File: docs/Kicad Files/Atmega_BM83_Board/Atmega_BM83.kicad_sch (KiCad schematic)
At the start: 7 parts, among them J1 Conn_01x12, J2 Conn_01x12, U1 ATmega328P-P

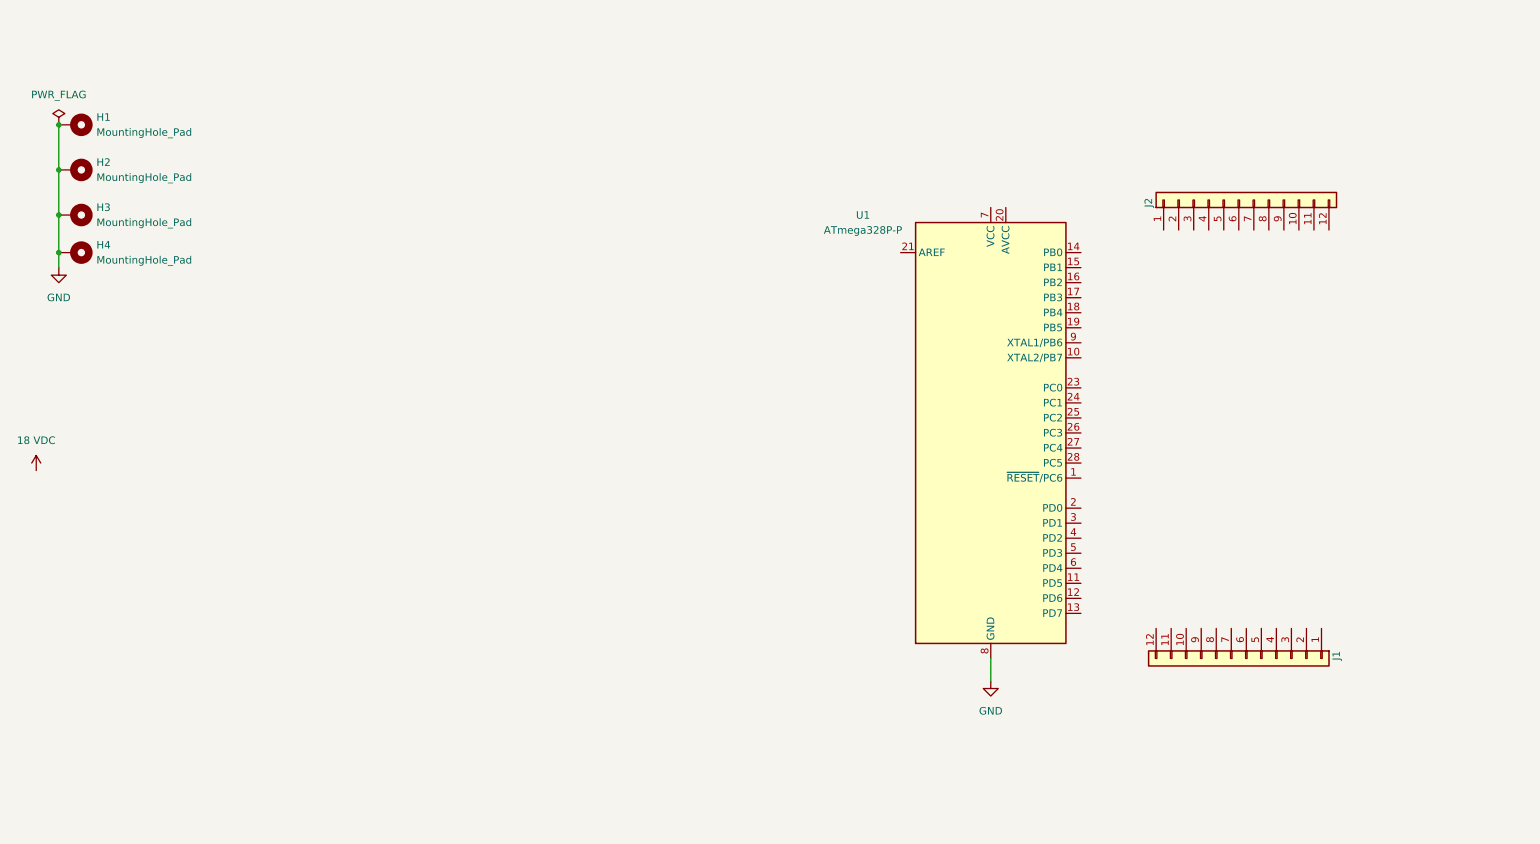
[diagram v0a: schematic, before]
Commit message: Added voltage divider
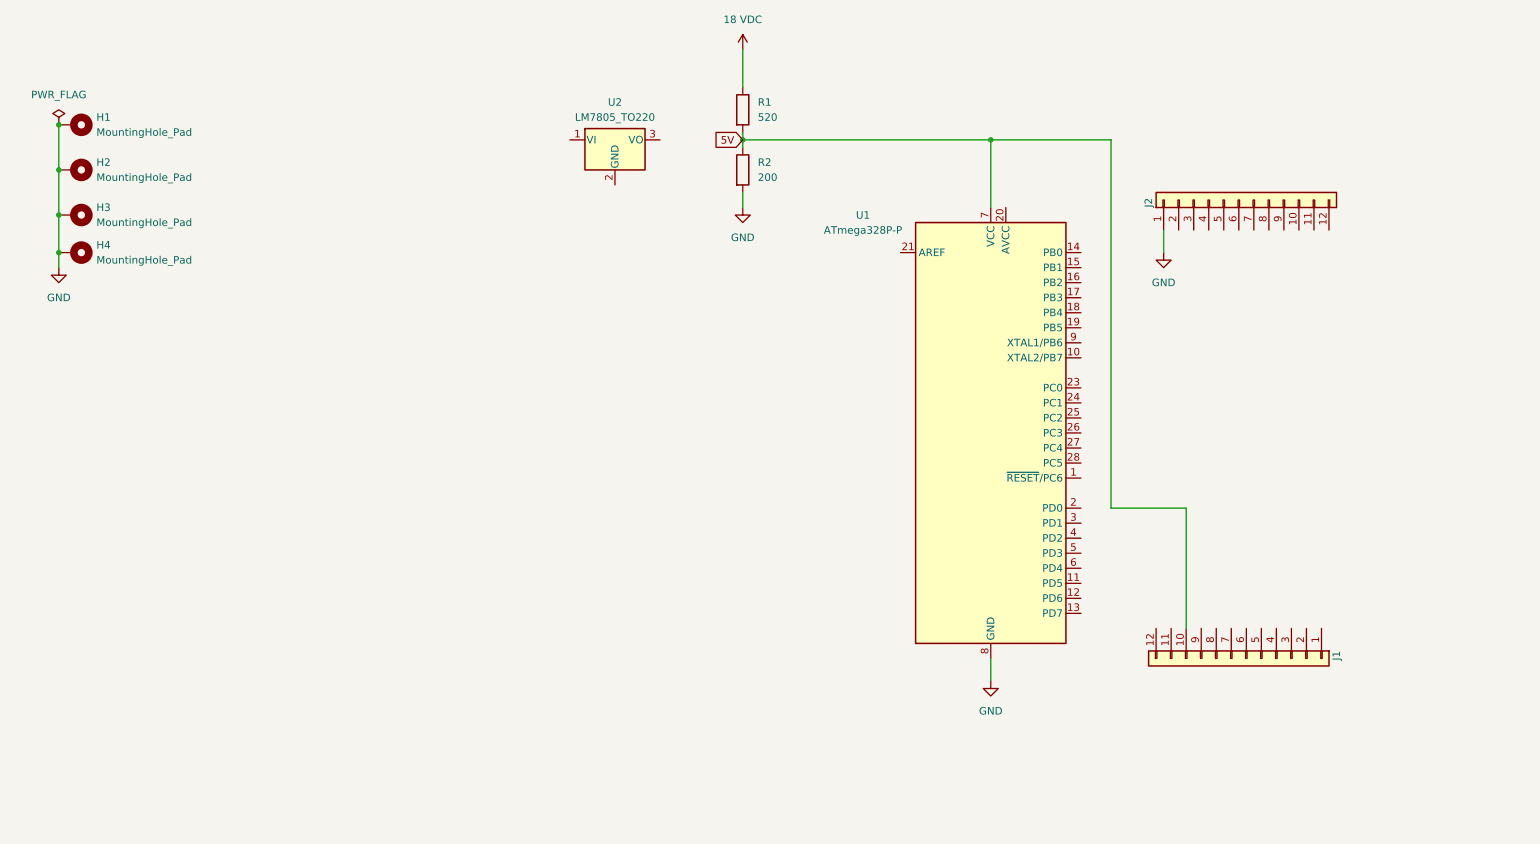
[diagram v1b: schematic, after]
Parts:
- added R1: 520, symbol Device:R
- added R2: 200, symbol Device:R
- added U2: LM7805_TO220, Package_TO_SOT_THT:TO-220-3_Vertical, symbol Regulator_Linear:LM7805_TO220
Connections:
- net 18 VDC: now also R1.1
- net GND: now also J2.1 (Pin_1), R2.2
- net 5V: now reaches J1.10 (Pin_10)
- net 5V: now also U1.7 (VCC), R1.2, R2.1

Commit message: updates for BM83/Atmega schematic
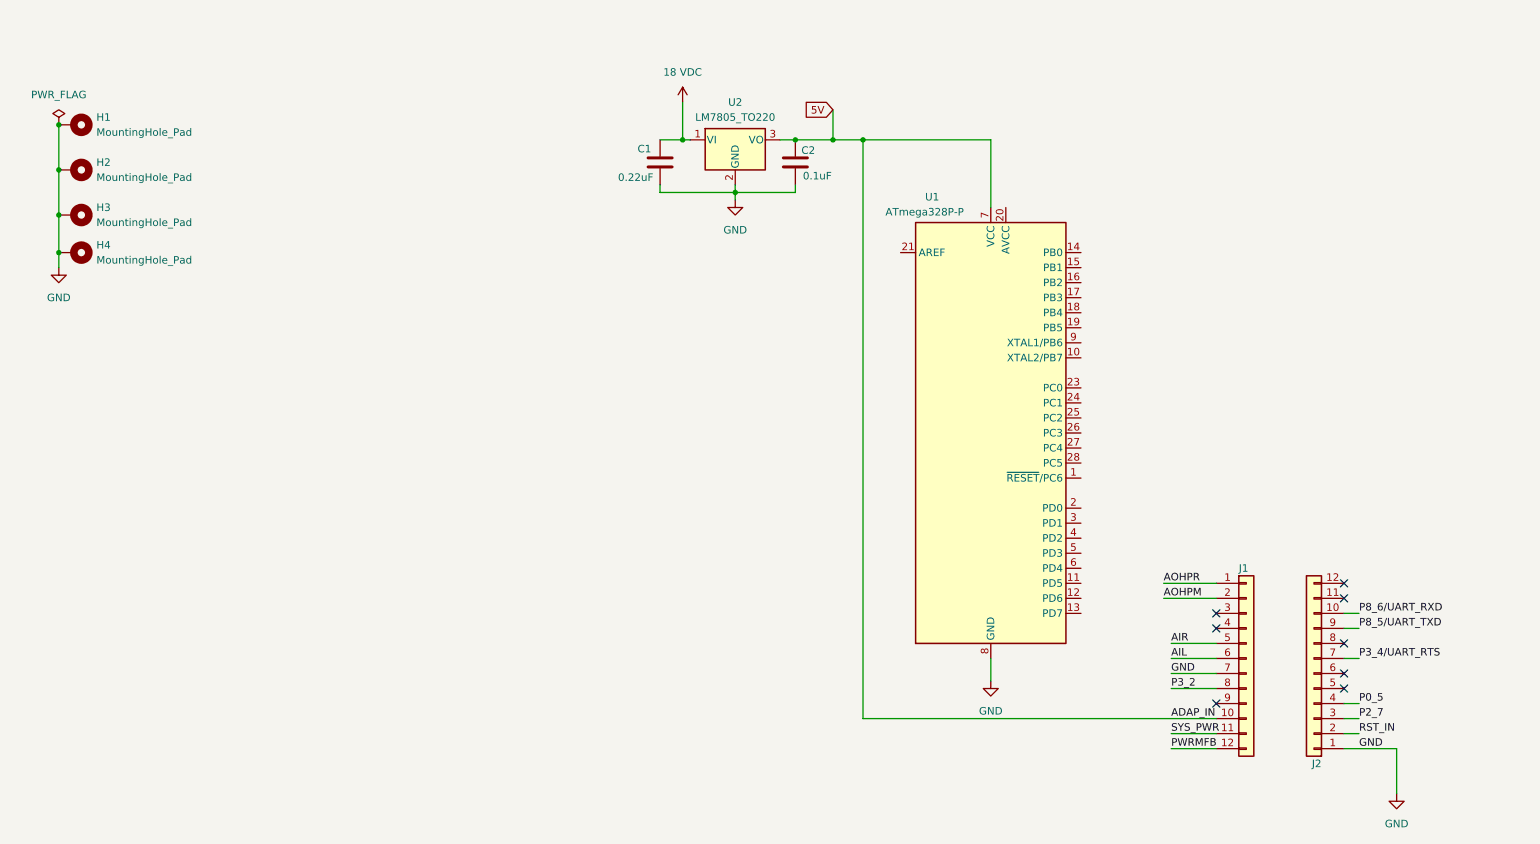
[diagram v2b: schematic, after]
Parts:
- removed R1: 520, symbol Device:R
- removed R2: 200, symbol Device:R
- added C1: 0.22uF, symbol Device:C
- added C2: 0.1uF, symbol Device:C
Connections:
- net 18 VDC: now also U2.1 (VI), C1.1
- net 5V: now also U2.3 (VO), C2.1
- net GND: now also J1.7 (Pin_7), U2.2 (GND), C1.2, C2.2
- net P8_6/UART_RXD: now reaches J2.10 (Pin_10)
- net RST_IN: now reaches J2.2 (Pin_2)
- net P2_7: now reaches J2.3 (Pin_3)
- net P0_5: now reaches J2.4 (Pin_4)
- net P3_4/UART_RTS: now reaches J2.7 (Pin_7)
- net P8_5/UART_TXD: now reaches J2.9 (Pin_9)
- net AOHPR: now reaches J1.1 (Pin_1)
- net SYS_PWR: now reaches J1.11 (Pin_11)
- net PWRMFB: now reaches J1.12 (Pin_12)
- net AOHPM: now reaches J1.2 (Pin_2)
- net AIR: now reaches J1.5 (Pin_5)
- net AIL: now reaches J1.6 (Pin_6)
- net P3_2: now reaches J1.8 (Pin_8)
- no-connect marks 0 -> 8
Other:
- moved on the sheet: J1, J2, U2

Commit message: more work on BM83/Atmega schematic
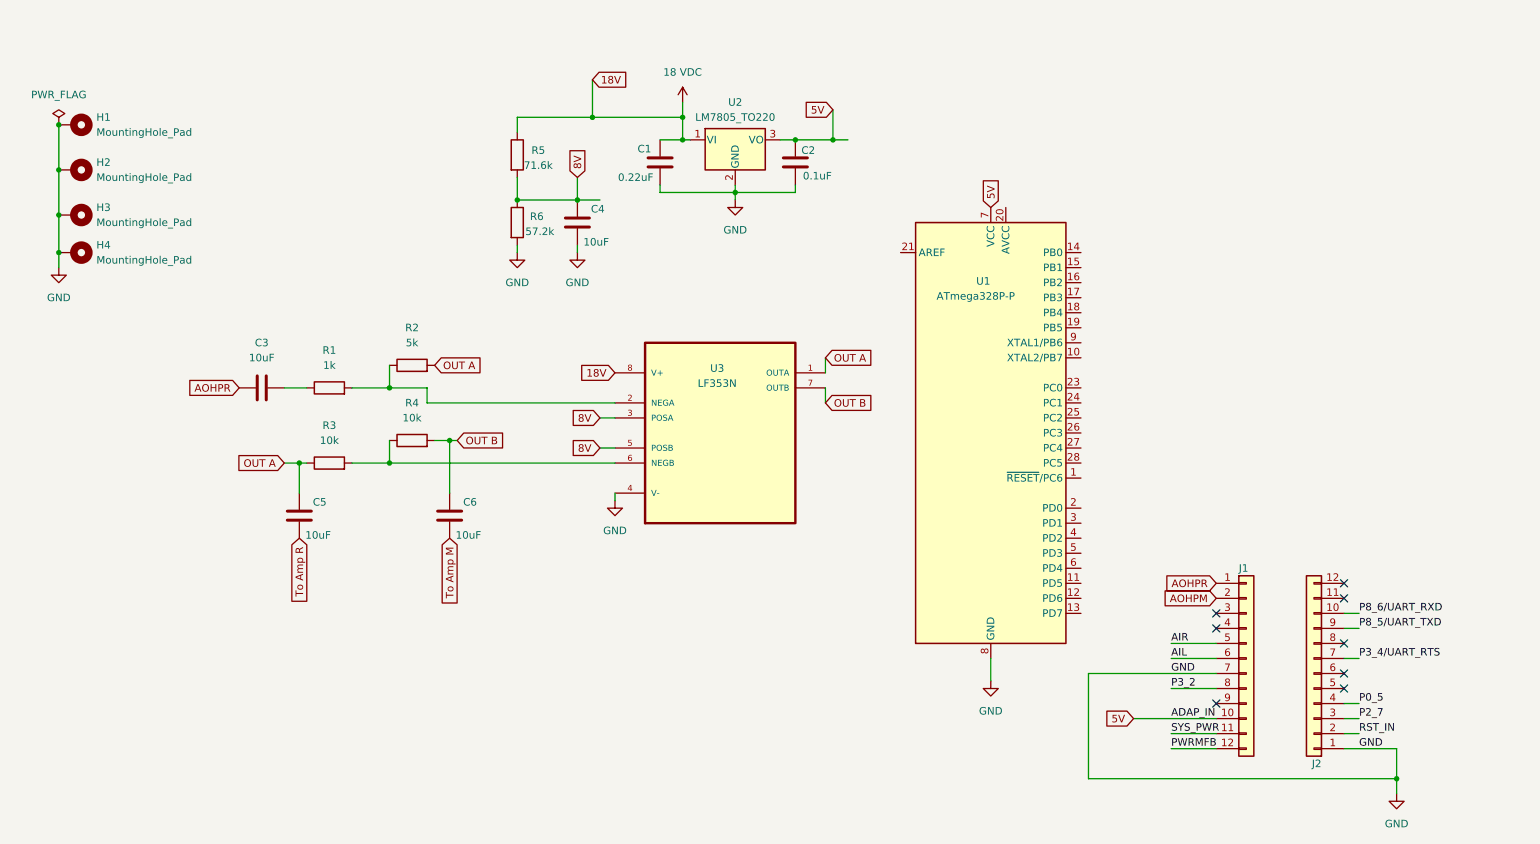
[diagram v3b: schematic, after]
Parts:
- added C3, C4, C5, C6: 10uF, symbol Device:C
- added R1: 1k, symbol Device:R
- added R2: 5k, symbol Device:R
- added R3, R4: 10k, symbol Device:R
- added R5: 71.6k, symbol Device:R
- added R6: 57.2k, symbol Device:R
- added U3: LF353N, Z_Custom_Footprints:LF353, symbol LF353N:LF353N
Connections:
- net 18 VDC: now also R5.1, U3.8 (V+)
- net AOHPR: now also C3.1
- net GND: now also C4.1, R6.2, U3.4 (V-)
- new net: R3.2, R4.1, U3.6 (NEGB)
- new net: R1.2, R2.1, U3.2 (NEGA)
- new net: C3.2, R1.1
- new net 8V: C4.2, R5.2, R6.1, U3.3 (POSA), U3.5 (POSB)
- new net OUT A: C5.2, R2.2, R3.1, U3.1 (OUTA)
- new net OUT B: C6.2, R4.2, U3.7 (OUTB)
- new net To Amp M: C6.1
- new net To Amp R: C5.1

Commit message: more work on BM83/Atmega schematic
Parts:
- added R7, R8: ~, symbol Device:R
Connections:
- net 18 VDC: now also R7.1; no longer U3.8 (V+)
- net GND: now also R8.2
- new net 16V: R7.2, R8.1, U3.8 (V+)

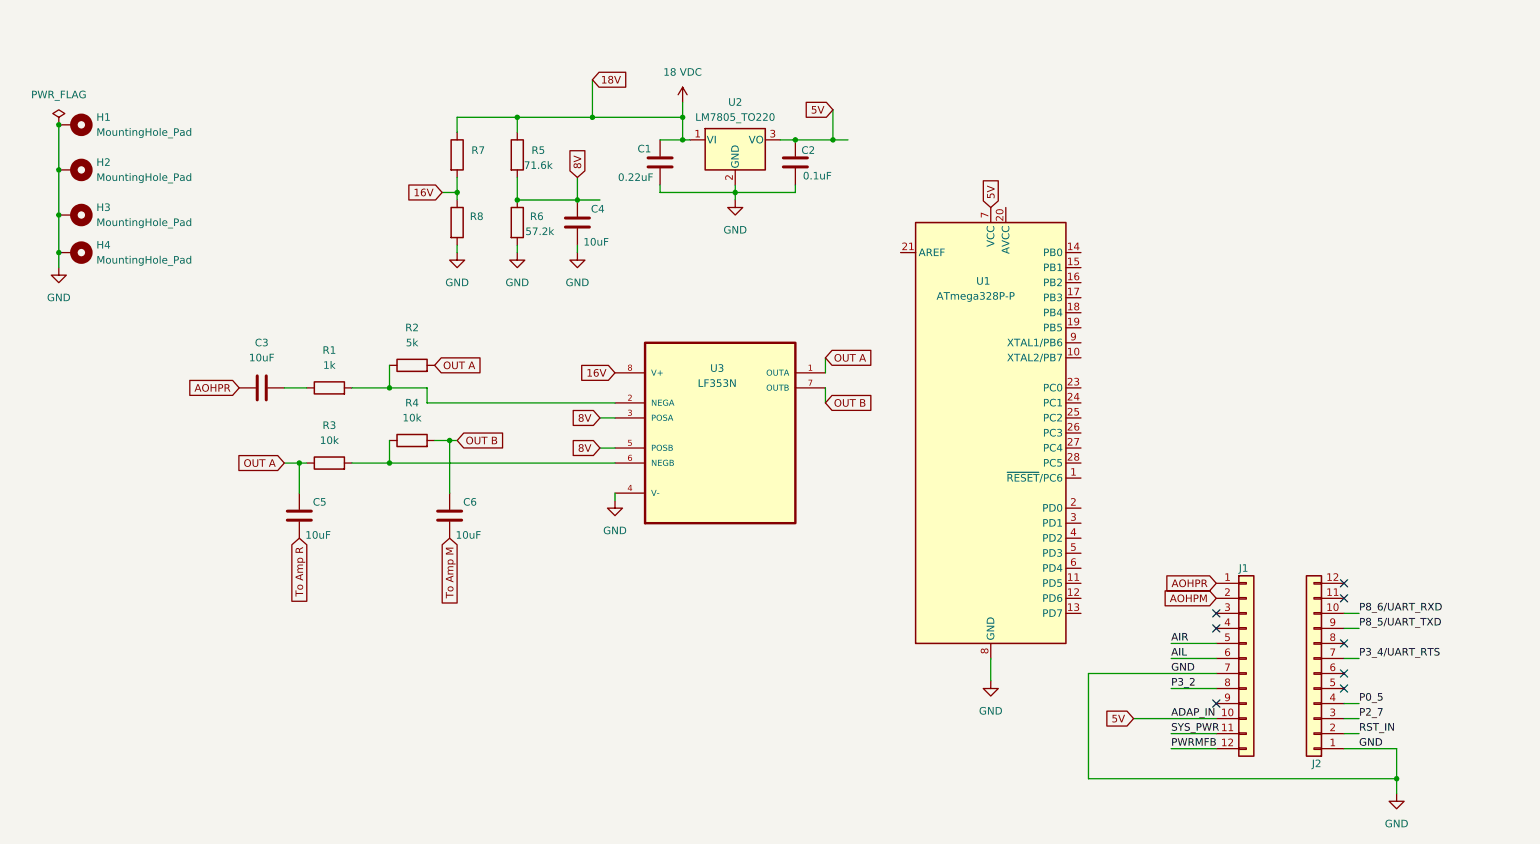
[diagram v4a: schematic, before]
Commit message: more work on Atmega/BM83 schematic
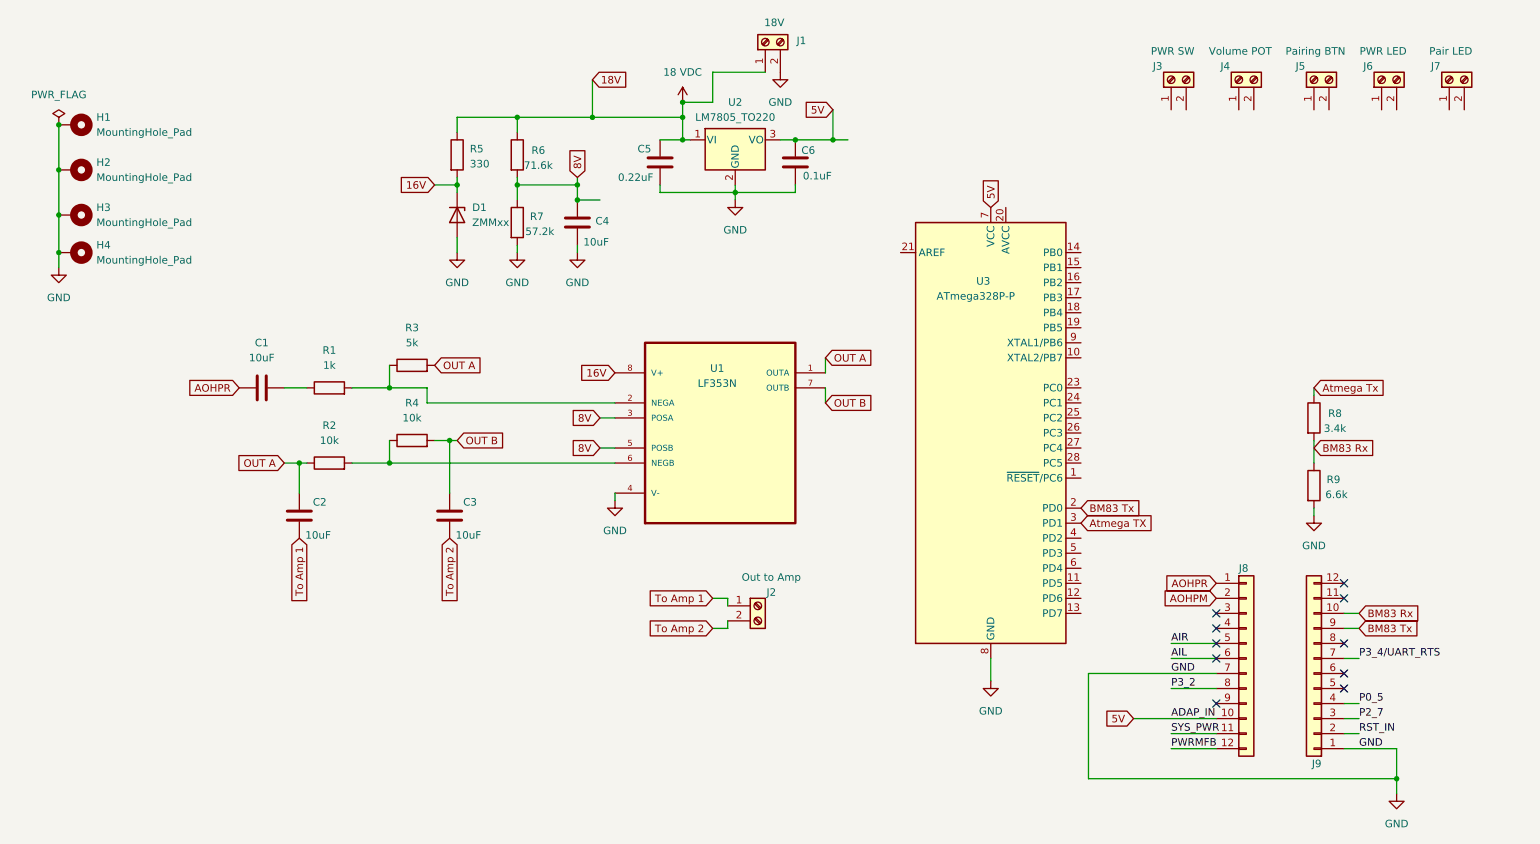
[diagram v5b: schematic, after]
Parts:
- removed R7: ~, symbol Device:R
- added D1: ZMMxx, Diode_SMD:D_MiniMELF, symbol Diode:ZMMxx
- added J1: 18V, TerminalBlock_Phoenix:TerminalBlock_Phoenix_MKDS-1,5-2_1x02_P5.00mm_Horizontal, symbol Connector:Screw_Terminal_01x02
- added J2: Out to Amp, TerminalBlock_Phoenix:TerminalBlock_Phoenix_MKDS-1,5-2_1x02_P5.00mm_Horizontal, symbol Connector:Screw_Terminal_01x02
- added J3: PWR SW, TerminalBlock_Phoenix:TerminalBlock_Phoenix_MKDS-1,5-2_1x02_P5.00mm_Horizontal, symbol Connector:Screw_Terminal_01x02
- added J4: Volume POT, TerminalBlock_Phoenix:TerminalBlock_Phoenix_MKDS-1,5-2_1x02_P5.00mm_Horizontal, symbol Connector:Screw_Terminal_01x02
- added J5: Pairing BTN, TerminalBlock_Phoenix:TerminalBlock_Phoenix_MKDS-1,5-2_1x02_P5.00mm_Horizontal, symbol Connector:Screw_Terminal_01x02
- added J6: PWR LED, TerminalBlock_Phoenix:TerminalBlock_Phoenix_MKDS-1,5-2_1x02_P5.00mm_Horizontal, symbol Connector:Screw_Terminal_01x02
- added J7: Pair LED, TerminalBlock_Phoenix:TerminalBlock_Phoenix_MKDS-1,5-2_1x02_P5.00mm_Horizontal, symbol Connector:Screw_Terminal_01x02
- added R8: 3.4k, Resistor_THT:R_Axial_DIN0207_L6.3mm_D2.5mm_P10.16mm_Horizontal, symbol Device:R
- added R9: 6.6k, Resistor_THT:R_Axial_DIN0207_L6.3mm_D2.5mm_P10.16mm_Horizontal, symbol Device:R
- C5: renamed from C1; footprint (none) -> Capacitor_THT:C_Rect_L7.0mm_W3.5mm_P5.00mm
- R1, R4: footprint (none) -> Resistor_THT:R_Axial_DIN0207_L6.3mm_D2.5mm_P10.16mm_Horizontal
- R2: renamed from R3; footprint (none) -> Resistor_THT:R_Axial_DIN0207_L6.3mm_D2.5mm_P10.16mm_Horizontal
- R3: renamed from R2; footprint (none) -> Resistor_THT:R_Axial_DIN0207_L6.3mm_D2.5mm_P10.16mm_Horizontal
- R5: renamed from R8; value ~ -> 330; footprint (none) -> Resistor_THT:R_Axial_DIN0207_L6.3mm_D2.5mm_P10.16mm_Horizontal
- R6: renamed from R5; footprint (none) -> Resistor_THT:R_Axial_DIN0207_L6.3mm_D2.5mm_P10.16mm_Horizontal
- R7: renamed from R6; footprint (none) -> Resistor_THT:R_Axial_DIN0207_L6.3mm_D2.5mm_P10.16mm_Horizontal
- renumbered C3 to C1, C5 to C2, C6 to C3, C2 to C6, J1 to J8, J2 to J9, U3 to U1, U1 to U3
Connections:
- net P8_5/UART_TXD is gone; now on net BM83 Tx: J9.9 (Pin_9)
- net 16V: now also R5.2, D1.1 (K); no longer R5.1
- net 18 VDC: now also R5.1, J1.1 (Pin_1)
- net GND: now also D1.2 (A), J1.2 (Pin_2), R9.2; no longer R5.2
- net BM83 Tx: now reaches U3.2 (PD0)
- net Atmega TX: now reaches U3.3 (PD1)
- net P8_6/UART_RXD renamed BM83 Rx
- net BM83 Rx: now also R8.2, R9.1
- net To Amp M renamed To Amp 2
- net To Amp 2: now also J2.2 (Pin_2)
- net To Amp R renamed To Amp 1
- net To Amp 1: now also J2.1 (Pin_1)
- new net Atmega Tx: R8.1
- no-connect marks 8 -> 10
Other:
- moved on the sheet: R5
